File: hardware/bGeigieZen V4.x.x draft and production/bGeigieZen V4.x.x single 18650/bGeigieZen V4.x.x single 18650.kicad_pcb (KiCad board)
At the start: 2 copper layers, 129.4 x 64.6 mm, 14 parts, among them J1 M5 2x15 pin, J2 Geiger IRover, J3 GPS, J4 Geiger Safepulse, J5 Extra support header, SW1 SW_SPDT

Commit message: Added some small changes to board V4.0.5 NFW
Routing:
- net /BAT: track 64.6 -> 63.1 mm
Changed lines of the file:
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@@
 	)
 	(segment
-		(start 114.941 115.746)
-		(end 114.862 115.825)
+		(start 155.0416 117.7179)
+		(end 155.0416 119.9376)
 		(width 0.5)
 		(layer "B.Cu")
@@
 	)
 	(segment
-		(start 116.411 112.846)
-		(end 151.971 112.846)
+		(start 155.0416 119.9376)
+		(end 156.8556 121.7516)
 		(width 0.5)
 		(layer "B.Cu")
@@
 	)
 	(segment
-		(start 151.971 114.429)
-		(end 159.294 121.752)
-		(width 0.5)
-		(layer "B.Cu")
-		(net 27)
-	)
-	(segment
-		(start 115.011 114.246)
-		(end 116.411 112.846)
+		(start 114.862 115.825)
+		(end 114.7043 115.825)
 		(width 0.5)
 		(layer "B.Cu")
@@
 	)
 	(segment
-		(start 167.678 122.877)
-		(end 168.053 123.252)
+		(start 116.2173 113.3844)
+		(end 150.7081 113.3844)
 		(width 0.5)
 		(layer "B.Cu")
@@
 	)
 	(segment
-		(start 151.971 112.846)
-		(end 151.971 114.429)
+		(start 114.7043 115.825)
+		(end 114.6253 115.746)
+		(width 0.5)
+		(layer "B.Cu")
+		(net 27)
+	)
+	(segment
+		(start 166.5526 121.7516)
+		(end 168.428 123.627)
 		(width 0.5)
 		(layer "B.Cu")
@@
 	)
 	(segment
-		(start 166.553 121.752)
-		(end 167.678 122.877)
+		(start 114.6253 114.9764)
+		(end 116.2173 113.3844)
 		(width 0.5)
 		(layer "B.Cu")
@@
 	)
 	(segment
-		(start 115.011 117.245)
-		(end 115.011 115.746)
+		(start 114.6253 115.746)
+		(end 114.6253 114.9764)
 		(width 0.5)
 		(layer "B.Cu")
@@
 	)
 	(segment
-		(start 115.011 115.746)
-		(end 114.941 115.746)
+		(start 150.7081 113.3844)
+		(end 155.0416 117.7179)
 		(width 0.5)
 		(layer "B.Cu")
@@
 	)
 	(segment
-		(start 168.053 123.252)
-		(end 168.428 123.627)
-		(width 0.5)
-		(layer "B.Cu")
-		(net 27)
-	)
-	(segment
-		(start 159.294 121.752)
-		(end 166.553 121.752)
+		(start 156.8556 121.7516)
+		(end 166.5526 121.7516)
 		(width 0.5)
 		(layer "B.Cu")
@@
 		(width 0.5)
 		(layer "B.Cu")
-		(net 27)
-	)
-	(segment
-		(start 115.011 115.746)
-		(end 115.011 114.246)
-		(width 0.5)
-		(layer "B.Cu")

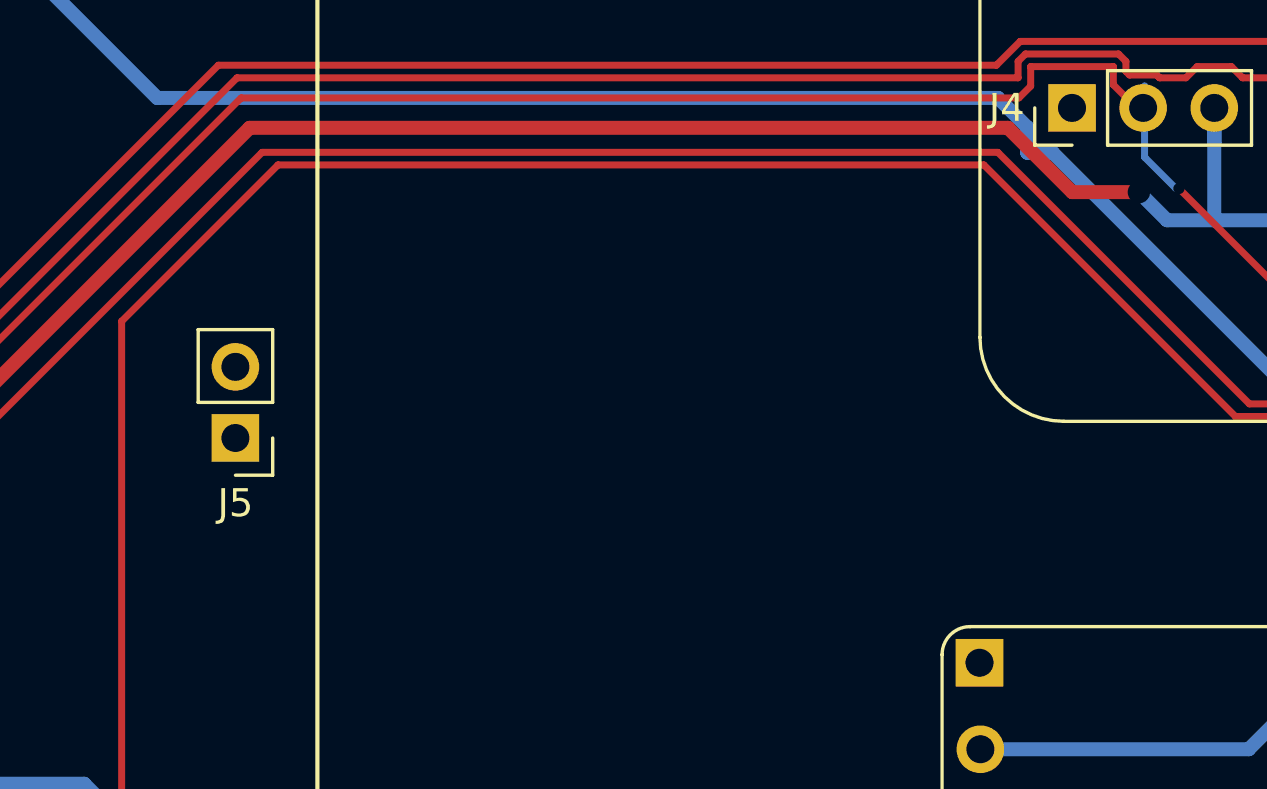
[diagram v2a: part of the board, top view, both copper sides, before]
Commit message: Updated footprints for the Safepulse on 4.x.x boards
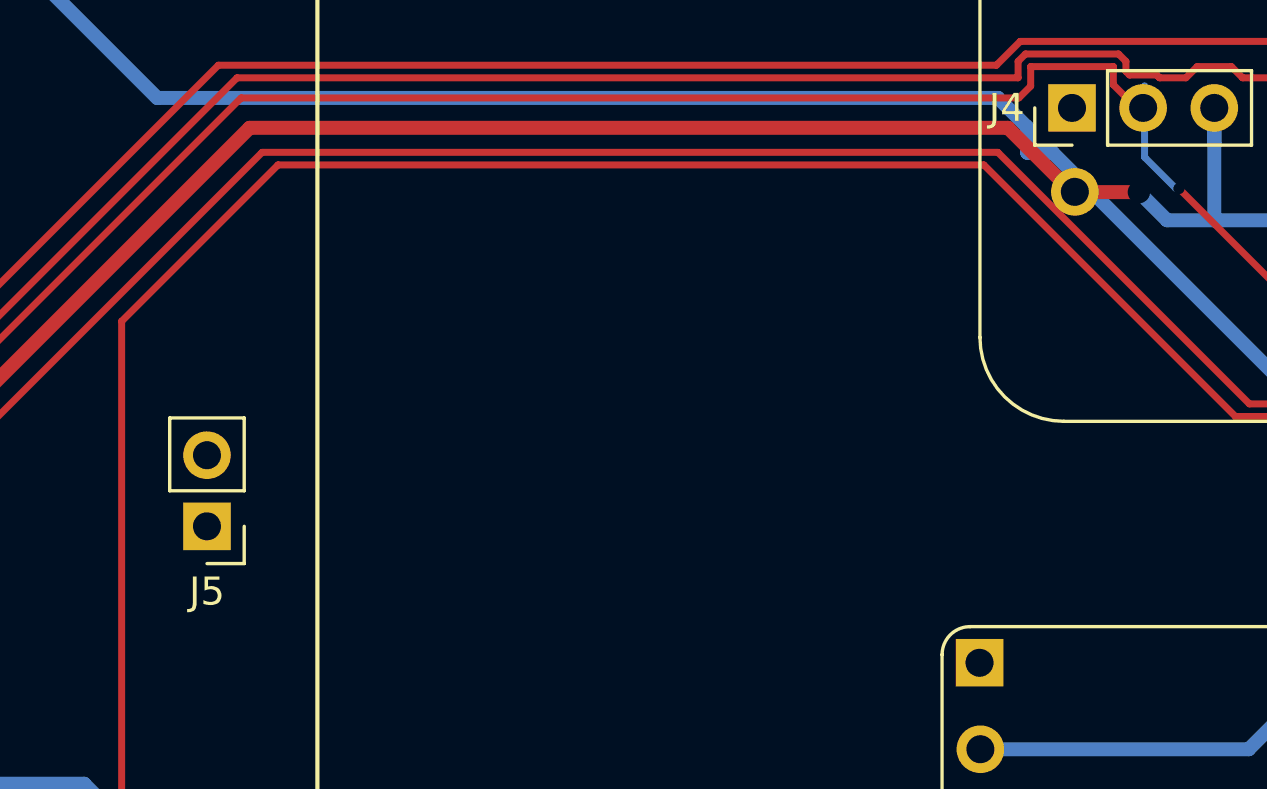
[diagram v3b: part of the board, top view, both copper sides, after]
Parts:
- added ?: , , F.Cu at (186.1, 92.3)
- moved J5 3.31 mm to (155.1, 104.2)
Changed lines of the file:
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@@
 		)
 	)
+	(footprint ""
+		(layer "F.Cu")
+		(at 186.0804 92.2516 180)
+		(property "Reference" ""
+			(at 0 0 360)
+			(layer "F.SilkS")
+			(effects
+				(font
+					(size 1.27 1.27)
+					(thickness 0.15)
+				)
+			)
+		)
+		(property "Value" ""
+			(at 0 0 360)
+			(layer "F.Fab")
+			(effects
+				(font
+					(size 1.27 1.27)
+					(thickness 0.15)
+				)
+			)
+		)
+		(property "Footprint" ""
+			(at 0 0 360)
+			(layer "F.Fab")
+			(hide yes)
+			(effects
+				(font
+					(size 1.27 1.27)
+					(thickness 0.15)
+				)
+			)
+		)
+		(property "Datasheet" ""
+			(at 0 0 360)
+			(layer "F.Fab")
+			(hide yes)
+			(effects
+				(font
+					(size 1.27 1.27)
+					(thickness 0.15)
+				)
+			)
+		)
+		(property "Description" ""
+			(at 0 0 360)
+			(layer "F.Fab")
+			(hide yes)
+			(effects
+				(font
+					(size 1.27 1.27)
+					(thickness 0.15)
+				)
+			)
+		)
+		(pad "3" thru_hole oval
+			(at 0 0 270)
+			(size 1.7 1.7)
+			(drill 1)
+			(layers "*.Cu" "*.Mask")
+			(remove_unused_layers no)
+			(net 1 "GND")
+			(pinfunction "Pin_3")
+			(pintype "passive")
+		)
+	)
 	(footprint "Connector_PinHeader_2.54mm:PinHeader_1x02_P2.54mm_Vertical"
 		(layer "F.Cu")
-		(at 156.1084 101.04 180)
+		(at 155.0924 104.1946 180)
 		(descr "Through hole straight pin header, 1x02, 2.54mm pitch, single row")
 		(tags "Through hole pin header THT 1x02 2.54mm single row")
@@
 	)
 	(gr_line
-		(start 153.1366 102.2912)
-		(end 153.1366 88.9684)
+		(start 193.574986 104.5264)
+		(end 193.5226 101.9864)
+		(stroke
+			(width 0.12)
+			(type default)
+		)
+		(layer "B.SilkS")
+	)
+	(gr_line
+		(start 152.9334 101.9864)
+		(end 152.9334 88.6636)
 		(stroke
 			(width 0.12)
@@
 	)
 	(gr_arc
-		(start 155.1366 104.2912)
-		(mid 153.722386 103.705414)
-		(end 153.1366 102.2912)
+		(start 154.985786 106.5264)
+		(mid 153.571572 105.940614)
+		(end 152.985786 104.5264)
 		(stroke
 			(width 0.12)
@@
 	)
 	(gr_arc
-		(start 193.7258 102.2912)
-		(mid 193.140014 103.705414)
-		(end 191.7258 104.2912)
+		(start 193.574986 104.5264)
+		(mid 192.9892 105.940614)
+		(end 191.574986 106.5264)
 		(stroke
 			(width 0.12)
@@
 	)
 	(gr_arc
-		(start 153.1366 88.9684)
-		(mid 153.722386 87.554186)
-		(end 155.1366 86.9684)
+		(start 152.9334 88.6636)
+		(mid 153.519186 87.249386)
+		(end 154.9334 86.6636)
+		(stroke
+			(width 0.12)
+			(type default)
+		)
+		(layer "B.SilkS")
+	)
+	(gr_line
+		(start 193.5226 88.6636)
+		(end 193.5226 101.9864)
 		(stroke
 			(width 0.12)
@@
 	)
 	(gr_line
-		(start 193.7258 88.9684)
-		(end 193.7258 102.2912)
+		(start 152.9334 101.9864)
+		(end 152.985786 104.5264)
 		(stroke
 			(width 0.12)
@@
 	)
 	(gr_line
-		(start 155.1366 86.9684)
-		(end 191.7258 86.9684)
+		(start 154.9334 86.6636)
+		(end 191.5226 86.6636)
 		(stroke
 			(width 0.12)
@@
 	)
 	(gr_arc
-		(start 191.7258 86.9684)
-		(mid 193.140014 87.554186)
-		(end 193.7258 88.9684)
+		(start 191.5226 86.6636)
+		(mid 192.936814 87.249386)
+		(end 193.5226 88.6636)
 		(stroke
 			(width 0.12)
@@
 	)
 	(gr_line
-		(start 191.7258 104.2912)
-		(end 155.1366 104.2912)
+		(start 191.574986 106.5264)
+		(end 154.985786 106.5264)
 		(stroke
 			(width 0.12)
@@
 	)
 	(gr_text "Safepulse"
-		(at 177.4952 89.6608 0)
+		(at 177.292 89.356 0)
 		(layer "B.SilkS")
 		(effects
@@
 	)
 	(group ""
-		(members "2e1e894e-7567-4071-a668-46d6ebfb9665" "35e36128-6801-4c0a-8941-083c7e89a3d8"
-			"5f05a722-553c-4d30-8de3-d6298ff2b16e" "693bfb3e-6025-4ee9-a4ed-ac25da7d9da5"
-			"734542f1-9af4-4a1a-a0aa-203a1626f31a" "8103ad81-a648-46c1-a7d5-c4b623ea342d"
+		(members "0a1c2d0d-7b6e-4f1b-9d51-340d3921c4f8" "2e1e894e-7567-4071-a668-46d6ebfb9665"
+			"35e36128-6801-4c0a-8941-083c7e89a3d8" "5f05a722-553c-4d30-8de3-d6298ff2b16e"
+			"693bfb3e-6025-4ee9-a4ed-ac25da7d9da5" "734542f1-9af4-4a1a-a0aa-203a1626f31a"
+			"8103ad81-a648-46c1-a7d5-c4b623ea342d" "8b548ead-f47b-4d4f-8ea4-4d0f95ca6846"
 			"9ce7780d-eb87-463c-be14-50af85c17fdc" "aef80be5-6fb2-4a43-9f41-e8b5022bdc8e"
 			"e1a0cc2e-1057-4757-8a17-f759adb29c4b"

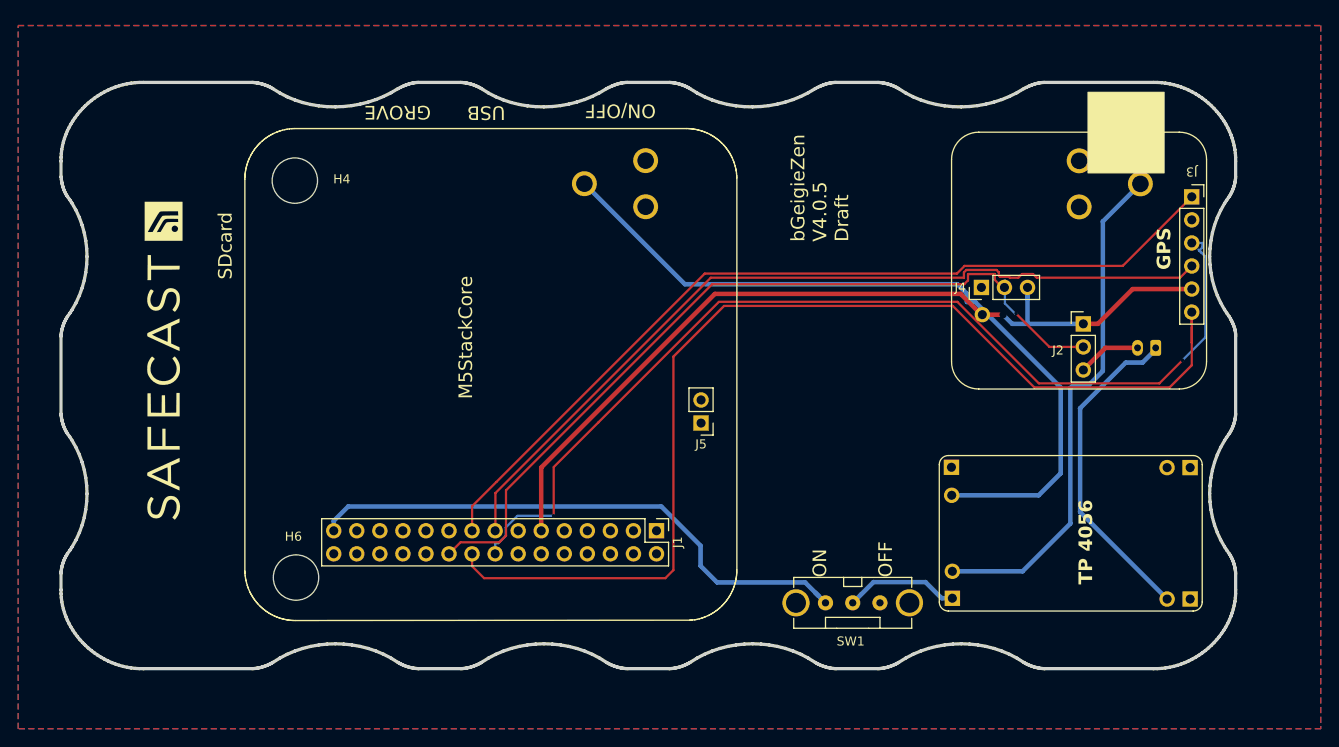
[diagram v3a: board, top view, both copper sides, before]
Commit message: Updated 4.x.x boards and 3.0.3a  with isolated positive battery for filling planes.
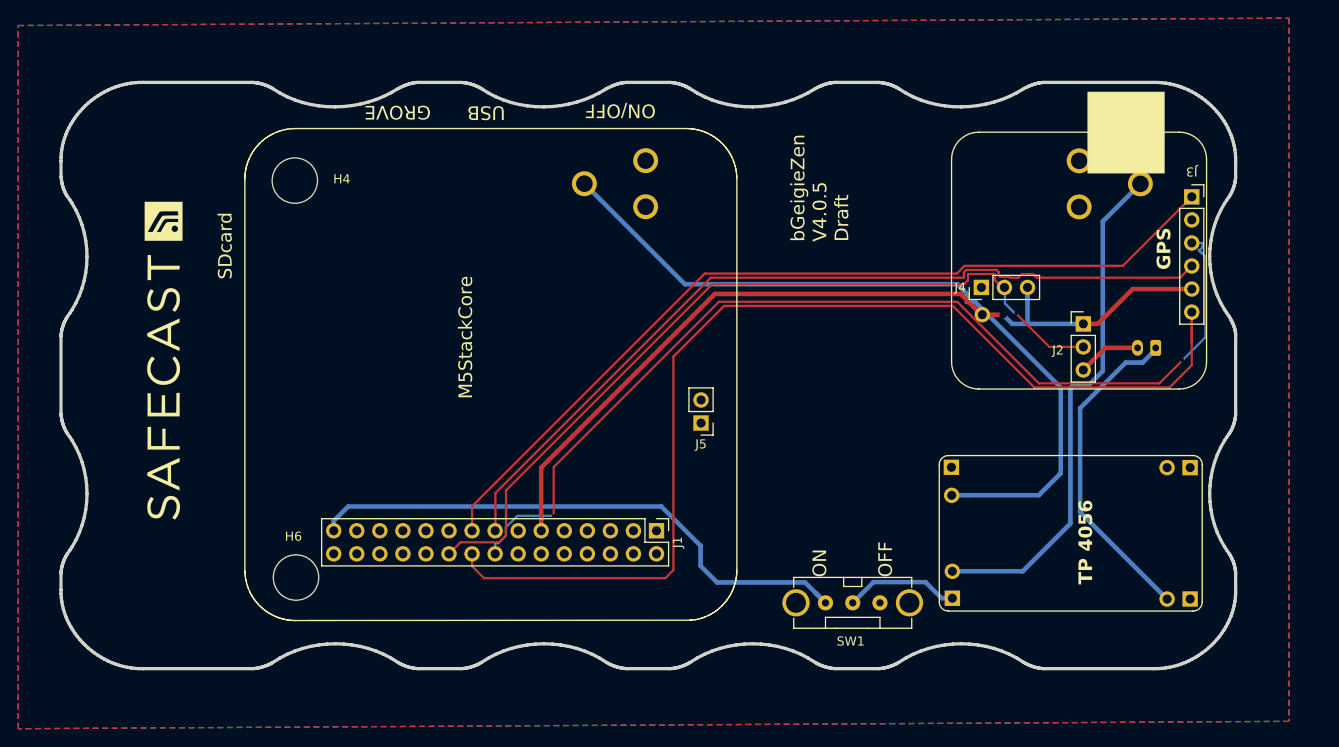
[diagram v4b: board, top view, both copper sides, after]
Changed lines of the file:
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@@
 (kicad_pcb
-	(version 20240225)
+	(version 20240609)
 	(generator "pcbnew")
 	(generator_version "8.99")
@@
 		(pad_to_mask_clearance 0)
 		(allow_soldermask_bridges_in_footprints no)
+		(tenting front back)
 		(aux_axis_origin 90.4338 71.8155)
 		(grid_origin 124.3076 84.53)
@@
 			(svgprecision 6)
 			(plotframeref no)
-			(viasonmask no)
 			(mode 1)
 			(useauxorigin no)
@@
 		(at 186.0804 92.2516 180)
 		(property "Reference" ""
-			(at 0 0 360)
+			(at 0 0 0)
 			(layer "F.SilkS")
 			(effects
@@
 		)
 		(property "Value" ""
-			(at 0 0 360)
+			(at 0 0 0)
 			(layer "F.Fab")
 			(effects
@@
 		)
 		(property "Footprint" ""
-			(at 0 0 360)
+			(at 0 0 0)
 			(layer "F.Fab")
 			(hide yes)
@@
 		)
 		(property "Datasheet" ""
-			(at 0 0 360)
+			(at 0 0 0)
 			(layer "F.Fab")
 			(hide yes)
@@
 		)
 		(property "Description" ""
-			(at 0 0 360)
+			(at 0 0 0)
 			(layer "F.Fab")
 			(hide yes)
@@
 		(drill 0.4)
 		(layers "F.Cu" "B.Cu")
+		(tenting none)
 		(net 3)
 	)
@@
 		(drill 0.4)
 		(layers "F.Cu" "B.Cu")
+		(tenting none)
 		(net 3)
 	)
@@
 		(drill 0.8)
 		(layers "F.Cu" "B.Cu")
+		(tenting none)
 		(net 4)
 	)
@@
 		(drill 0.4)
 		(layers "F.Cu" "B.Cu")
+		(tenting none)
 		(net 18)
 	)
@@
 	)
 	(zone
+		(net 0)
+		(net_name "")
+		(layers "F&B.Cu")
+		(hatch full 0.5)
+		(connect_pads
+			(clearance 0)
+		)
+		(min_thickness 0.25)
+		(filled_areas_thickness no)
+		(keepout
+			(tracks allowed)
+			(vias allowed)
+			(pads allowed)
+			(copperpour not_allowed)
+			(footprints allowed)
+		)
+		(fill
+			(thermal_gap 0.5)
+			(thermal_bridge_width 0.5)
+		)
+		(polygon
+			(pts
+				(xy 193.285801 71.211459) (xy 207.6704 71.1188) (xy 207.916201 83.860659) (xy 193.2432 83.7172)
+			)
+		)
+	)
+	(zone
 		(net 1)
 		(net_name "GND")
@@
 		(polygon
 			(pts
-				(xy 223.3676 60.4) (xy 223.3676 137.87) (xy 79.8576 137.87) (xy 79.8576 60.4)
+				(xy 219.8624 59.5872) (xy 219.8624 137.0572) (xy 79.8576 137.87) (xy 79.8576 60.4)
 			)
 		)

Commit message: Update V3.x.x and V4.x.x board with updated 18650 footprints.
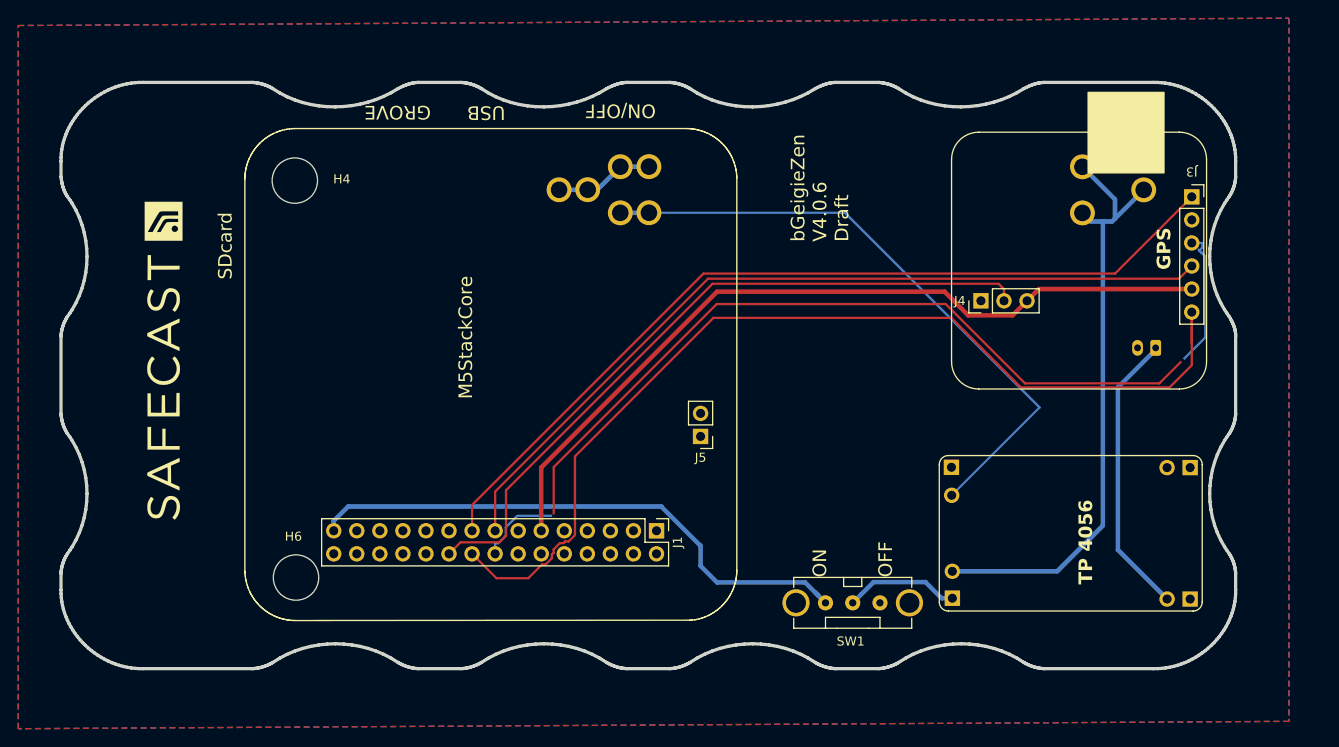
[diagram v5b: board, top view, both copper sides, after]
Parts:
- removed ?: , 
- removed J2: Geiger IRover, Connector_PinHeader_2.54mm:PinHeader_1x03_P2.54mm_Vertical
- BT1: value 3.7 V Lipo -> 3.7 V Lipo; footprint Library:BATTERY_18650-HOLDER -> bGeigieZen:BATTERY_18650-HOLDER
- moved J5 1.47 mm to (155.0, 105.7)
- moved J4 1.47 mm to (185.9, 90.7)
- moved BT1 0.75 mm to (173.2, 78.5)
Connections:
- BT1 pad GND@2: (no net) -> Net-(BT1--)
- BT1 pad GND@3: (no net) -> Net-(BT1--)
- BT1 pad PWR@2: (no net) -> Net-(BT1-+)
- BT1 pad PWR@3: (no net) -> Net-(BT1-+)
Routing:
- net /GIO2 on Core and GIO32 on Core-2: track 91.5 -> 78.2 mm, vias 1 -> 0
- net Net-(BT1-+): track 56.8 -> 67.9 mm
- net /SCL: track 120.1 -> 110.0 mm
- net GND: track 6.99 -> 0.00 mm
- net 3.3V: track 94.8 -> 88.9 mm, vias 1 -> 0
- net Net-(BT1--): track 84.8 -> 79.7 mm
- net Net-(QIcharger1-Pin_1): track 36.2 -> 31.7 mm
- net /RX2: track 93.1 -> 91.6 mm
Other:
- board text added: "bGeigieZen V4.0.6 Draft"
